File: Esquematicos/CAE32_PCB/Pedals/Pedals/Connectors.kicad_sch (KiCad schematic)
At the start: 3 parts, among them J10 ST-Link, J8 USB_C_Receptacle, J9 UART_PGR

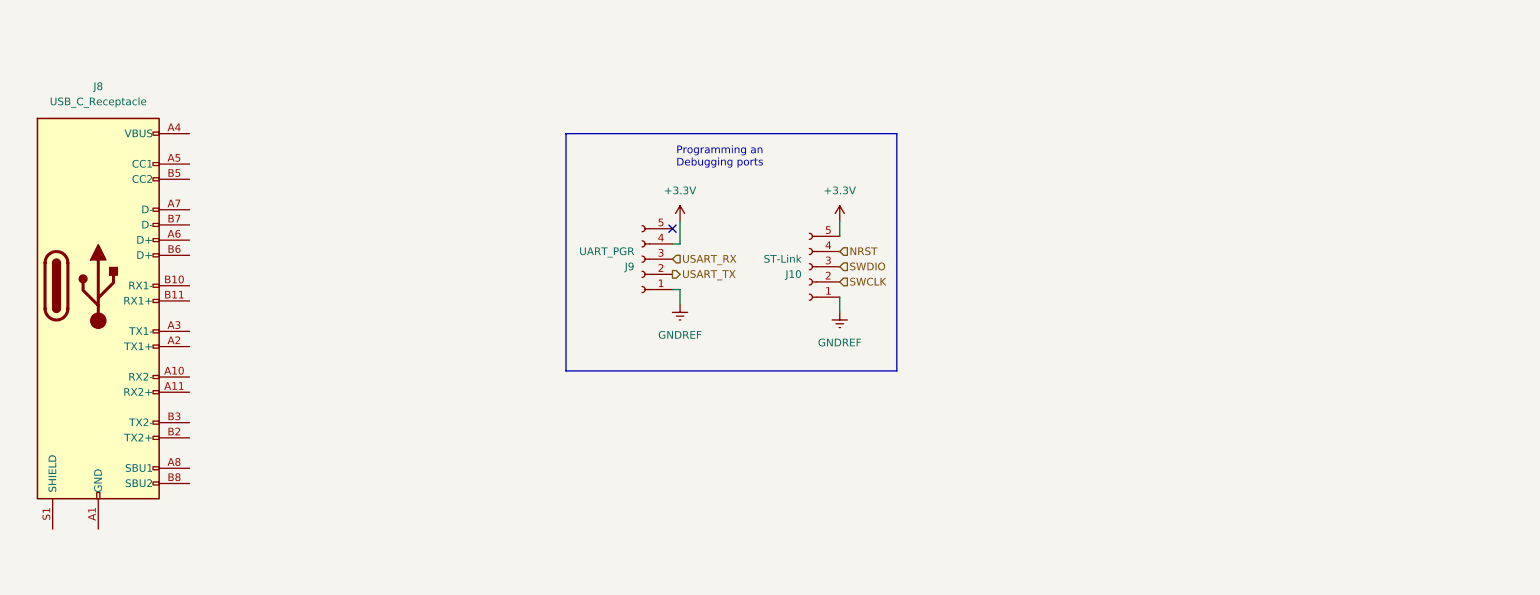
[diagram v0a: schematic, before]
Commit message: update: Primera revision de etapa ADC lista, ademas de una mejor distrubucion de componentes
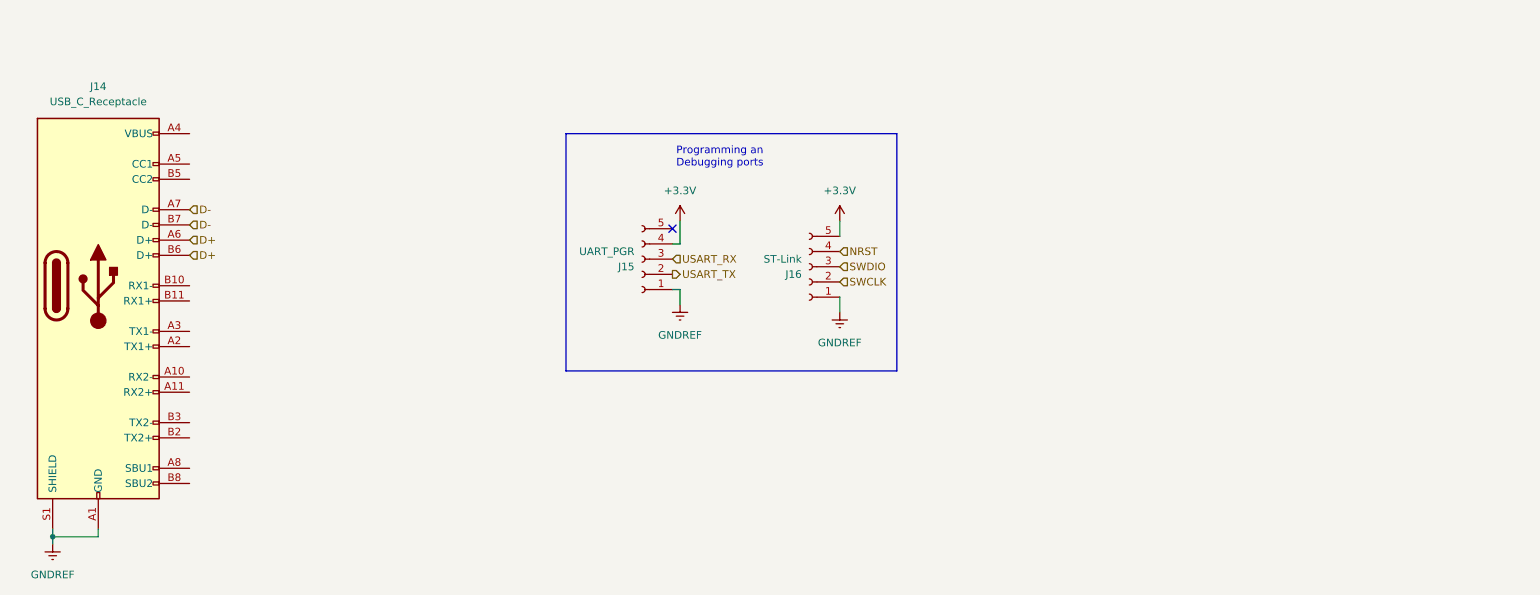
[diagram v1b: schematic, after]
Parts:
- renumbered J8 to J14, J9 to J15, J10 to J16
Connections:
- net GNDREF: now also J14.A1 (GND), J14.A12 (GND), J14.B1 (GND), J14.B12 (GND), J14.S1 (SHIELD)
- net D+: now reaches J14.A6 (D+)
- net D+: now also J14.B6 (D+)
- net D-: now reaches J14.A7 (D-)
- net D-: now also J14.B7 (D-)
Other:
- title: (none) -> CAE32 pedals
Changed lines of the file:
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@@
 (kicad_sch (version 20211123) (generator eeschema)
   (paper "A4")
+  (title_block
+    (title "CAE32 pedals")
+    (rev "2")
+    (comment 1 "Desing by: janc18")
+  )
+  (junction (at 33.655 102.87) (diameter 0) (color 0 0 0 0)
+  )
   (no_connect (at 137.16 51.435))
   (polyline (pts (xy 174.625 35.56) (xy 174.625 75.184))
@@
     (stroke (width 0) (type default) (color 0 0 0 0))
   )
+  (wire (pts (xy 33.655 101.6) (xy 33.655 102.87))
+    (stroke (width 0) (type default) (color 0 0 0 0))
+  )
   (polyline (pts (xy 119.38 75.184) (xy 174.625 75.184))
     (stroke (width 0) (type default) (color 0 0 0 0))
@@
     (stroke (width 0) (type default) (color 0 0 0 0))
   )
+  (wire (pts (xy 33.655 102.87) (xy 41.275 102.87))
+    (stroke (width 0) (type default) (color 0 0 0 0))
+  )
   (wire (pts (xy 138.43 64.135) (xy 138.43 61.595))
     (stroke (width 0) (type default) (color 0 0 0 0))
@@
     (stroke (width 0) (type default) (color 0 0 0 0))
   )
+  (wire (pts (xy 41.275 101.6) (xy 41.275 102.87))
+    (stroke (width 0) (type default) (color 0 0 0 0))
+  )
   (wire (pts (xy 165.1 50.165) (xy 165.1 52.705))
+    (stroke (width 0) (type default) (color 0 0 0 0))
+  )
+  (wire (pts (xy 33.655 102.87) (xy 33.655 104.14))
     (stroke (width 0) (type default) (color 0 0 0 0))
   )
@@
     (effects (font (size 1.27 1.27)) (justify left))
   )
+  (hierarchical_label "D-" (shape input) (at 56.515 48.26 0)
+    (effects (font (size 1.27 1.27)) (justify left))
+  )
   (hierarchical_label "NRST" (shape input) (at 165.1 55.245 0)
     (effects (font (size 1.27 1.27)) (justify left))
@@
     (effects (font (size 1.27 1.27)) (justify left))
   )
+  (hierarchical_label "D-" (shape input) (at 56.515 50.8 0)
+    (effects (font (size 1.27 1.27)) (justify left))
+  )
   (hierarchical_label "SWCLK" (shape input) (at 165.1 60.325 0)
     (effects (font (size 1.27 1.27)) (justify left))
   )
+  (hierarchical_label "D+" (shape input) (at 56.515 55.88 0)
+    (effects (font (size 1.27 1.27)) (justify left))
+  )
+  (hierarchical_label "D+" (shape input) (at 56.515 53.34 0)
+    (effects (font (size 1.27 1.27)) (justify left))
+  )
   (symbol (lib_id "power:GNDREF") (at 165.1 65.405 0) (unit 1)
     (in_bom yes) (on_board yes) (fields_autoplaced)
-    (property "Reference" "#PWR038" (id 0) (at 165.1 71.755 0)
+    (property "Reference" "#PWR053" (id 0) (at 165.1 71.755 0)
       (effects (font (size 1.27 1.27)) hide)
     )
@@
   (symbol (lib_id "Connector:USB_C_Receptacle") (at 41.275 60.96 0) (unit 1)
     (in_bom yes) (on_board yes) (fields_autoplaced)
-    (property "Reference" "J8" (id 0) (at 41.275 27.686 0))
+    (property "Reference" "J14" (id 0) (at 41.275 27.686 0))
     (property "Value" "USB_C_Receptacle" (id 1) (at 41.275 30.226 0))
     (property "Footprint" "Connector_USB:USB_C_Receptacle_Amphenol_12401548E4-2A_CircularHoles" (id 2) (at 45.085 60.96 0)
@@
   (symbol (lib_id "power:GNDREF") (at 138.43 64.135 0) (unit 1)
     (in_bom yes) (on_board yes) (fields_autoplaced)
-    (property "Reference" "#PWR036" (id 0) (at 138.43 70.485 0)
+    (property "Reference" "#PWR051" (id 0) (at 138.43 70.485 0)
       (effects (font (size 1.27 1.27)) hide)
     )
@@
   (symbol (lib_id "power:+3.3V") (at 138.43 50.165 0) (unit 1)
     (in_bom yes) (on_board yes) (fields_autoplaced)
-    (property "Reference" "#PWR035" (id 0) (at 138.43 53.975 0)
+    (property "Reference" "#PWR050" (id 0) (at 138.43 53.975 0)
       (effects (font (size 1.27 1.27)) hide)
     )
@@
     (pin "1")
   )
+  (symbol (lib_name "GNDREF_1") (lib_id "power:GNDREF") (at 33.655 104.14 0) (unit 1)
+    (in_bom yes) (on_board yes) (fields_autoplaced)
+    (property "Reference" "#PWR049" (id 0) (at 33.655 110.49 0)
+      (effects (font (size 1.27 1.27)) hide)
+    )
+    (property "Value" "GNDREF" (id 1) (at 33.655 109.22 0))
+    (property "Footprint" "" (id 2) (at 33.655 104.14 0)
+      (effects (font (size 1.27 1.27)) hide)
+    )
+    (property "Datasheet" "" (id 3) (at 33.655 104.14 0)
+      (effects (font (size 1.27 1.27)) hide)
+    )
+    (pin "1")
+  )
   (symbol (lib_id "power:+3.3V") (at 165.1 50.165 0) (unit 1)
     (in_bom yes) (on_board yes) (fields_autoplaced)
-    (property "Reference" "#PWR037" (id 0) (at 165.1 53.975 0)
+    (property "Reference" "#PWR052" (id 0) (at 165.1 53.975 0)
       (effects (font (size 1.27 1.27)) hide)
     )
@@
   (symbol (lib_id "Connector:Conn_01x05_Female") (at 132.08 56.515 180) (unit 1)
     (in_bom yes) (on_board yes)
-    (property "Reference" "J9" (id 0) (at 130.81 57.7851 0)
+    (property "Reference" "J15" (id 0) (at 130.81 57.7851 0)
       (effects (font (size 1.27 1.27)) (justify left))
     )
@@
   (symbol (lib_id "Connector:Conn_01x05_Female") (at 160.02 57.785 180) (unit 1)
     (in_bom yes) (on_board yes)
-    (property "Reference" "J10" (id 0) (at 158.75 59.0551 0)
+    (property "Reference" "J16" (id 0) (at 158.75 59.0551 0)
       (effects (font (size 1.27 1.27)) (justify left))
     )

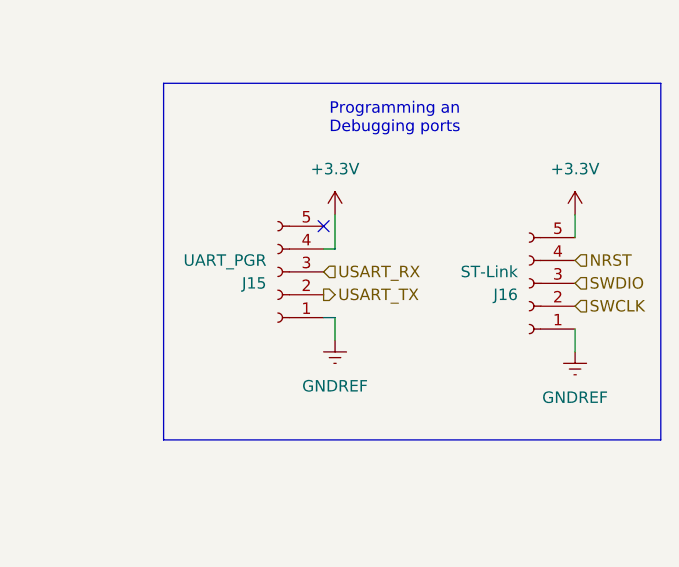
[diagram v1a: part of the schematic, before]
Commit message: update: se añade otra hoja para las celdas de carga, ademas de reorganizar todas las hojas
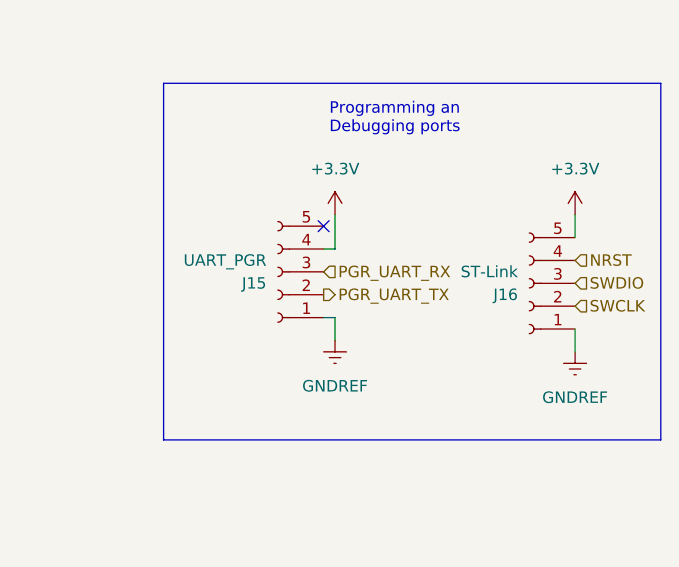
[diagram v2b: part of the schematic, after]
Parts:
- J14: footprint Connector_USB:USB_C_Receptacle_Amphenol_12401548E4-2A_CircularHoles -> Connector_USB:USB_C_Receptacle_G-Switch_GT-USB-7010ASV
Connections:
- net USART_RX renamed PGR_UART_RX
- net USART_TX renamed PGR_UART_TX
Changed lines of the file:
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@@
     (effects (font (size 1.27 1.27)) (justify left bottom))
   )
-  (hierarchical_label "USART_TX" (shape output) (at 137.16 59.055 0)
+  (hierarchical_label "PGR_UART_TX" (shape output) (at 137.16 59.055 0)
     (effects (font (size 1.27 1.27)) (justify left))
   )
@@
     (effects (font (size 1.27 1.27)) (justify left))
   )
-  (hierarchical_label "USART_RX" (shape input) (at 137.16 56.515 0)
+  (hierarchical_label "PGR_UART_RX" (shape input) (at 137.16 56.515 0)
     (effects (font (size 1.27 1.27)) (justify left))
   )
@@
   (symbol (lib_id "power:GNDREF") (at 165.1 65.405 0) (unit 1)
     (in_bom yes) (on_board yes) (fields_autoplaced)
-    (property "Reference" "#PWR053" (id 0) (at 165.1 71.755 0)
+    (property "Reference" "#PWR045" (id 0) (at 165.1 71.755 0)
       (effects (font (size 1.27 1.27)) hide)
     )
@@
     (property "Reference" "J14" (id 0) (at 41.275 27.686 0))
     (property "Value" "USB_C_Receptacle" (id 1) (at 41.275 30.226 0))
-    (property "Footprint" "Connector_USB:USB_C_Receptacle_Amphenol_12401548E4-2A_CircularHoles" (id 2) (at 45.085 60.96 0)
+    (property "Footprint" "Connector_USB:USB_C_Receptacle_G-Switch_GT-USB-7010ASV" (id 2) (at 45.085 60.96 0)
       (effects (font (size 1.27 1.27)) hide)
     )
@@
   (symbol (lib_id "power:GNDREF") (at 138.43 64.135 0) (unit 1)
     (in_bom yes) (on_board yes) (fields_autoplaced)
-    (property "Reference" "#PWR051" (id 0) (at 138.43 70.485 0)
+    (property "Reference" "#PWR043" (id 0) (at 138.43 70.485 0)
       (effects (font (size 1.27 1.27)) hide)
     )
@@
   (symbol (lib_id "power:+3.3V") (at 138.43 50.165 0) (unit 1)
     (in_bom yes) (on_board yes) (fields_autoplaced)
-    (property "Reference" "#PWR050" (id 0) (at 138.43 53.975 0)
+    (property "Reference" "#PWR042" (id 0) (at 138.43 53.975 0)
       (effects (font (size 1.27 1.27)) hide)
     )
@@
   (symbol (lib_name "GNDREF_1") (lib_id "power:GNDREF") (at 33.655 104.14 0) (unit 1)
     (in_bom yes) (on_board yes) (fields_autoplaced)
-    (property "Reference" "#PWR049" (id 0) (at 33.655 110.49 0)
+    (property "Reference" "#PWR041" (id 0) (at 33.655 110.49 0)
       (effects (font (size 1.27 1.27)) hide)
     )
@@
   (symbol (lib_id "power:+3.3V") (at 165.1 50.165 0) (unit 1)
     (in_bom yes) (on_board yes) (fields_autoplaced)
-    (property "Reference" "#PWR052" (id 0) (at 165.1 53.975 0)
+    (property "Reference" "#PWR044" (id 0) (at 165.1 53.975 0)
       (effects (font (size 1.27 1.27)) hide)
     )

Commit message: update: Componentes acomodados en la PCB
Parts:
- renumbered J14 to J15, J15 to J16, J16 to J17
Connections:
- net PGR_UART_RX: now also J16.2 (Pin_2); no longer J16.3 (Pin_3)
- net PGR_UART_TX: now also J16.3 (Pin_3); no longer J16.2 (Pin_2)
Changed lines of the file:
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@@
     (effects (font (size 1.27 1.27)) (justify left bottom))
   )
-  (hierarchical_label "PGR_UART_TX" (shape output) (at 137.16 59.055 0)
+  (hierarchical_label "PGR_UART_TX" (shape output) (at 137.16 56.515 0)
     (effects (font (size 1.27 1.27)) (justify left))
   )
@@
     (effects (font (size 1.27 1.27)) (justify left))
   )
-  (hierarchical_label "PGR_UART_RX" (shape input) (at 137.16 56.515 0)
+  (hierarchical_label "PGR_UART_RX" (shape input) (at 137.16 59.055 0)
     (effects (font (size 1.27 1.27)) (justify left))
   )
@@
   (symbol (lib_id "Connector:USB_C_Receptacle") (at 41.275 60.96 0) (unit 1)
     (in_bom yes) (on_board yes) (fields_autoplaced)
-    (property "Reference" "J14" (id 0) (at 41.275 27.686 0))
+    (property "Reference" "J15" (id 0) (at 41.275 27.686 0))
     (property "Value" "USB_C_Receptacle" (id 1) (at 41.275 30.226 0))
     (property "Footprint" "Connector_USB:USB_C_Receptacle_G-Switch_GT-USB-7010ASV" (id 2) (at 45.085 60.96 0)
@@
   (symbol (lib_id "Connector:Conn_01x05_Female") (at 132.08 56.515 180) (unit 1)
     (in_bom yes) (on_board yes)
-    (property "Reference" "J15" (id 0) (at 130.81 57.7851 0)
+    (property "Reference" "J16" (id 0) (at 130.81 57.7851 0)
       (effects (font (size 1.27 1.27)) (justify left))
     )
@@
   (symbol (lib_id "Connector:Conn_01x05_Female") (at 160.02 57.785 180) (unit 1)
     (in_bom yes) (on_board yes)
-    (property "Reference" "J16" (id 0) (at 158.75 59.0551 0)
+    (property "Reference" "J17" (id 0) (at 158.75 59.0551 0)
       (effects (font (size 1.27 1.27)) (justify left))
     )

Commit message: update: se agrega el consumo de corriente a los IC's ademas de agregar el URL y numero de parte de los componentes de LCSC en kicad
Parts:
- J16, J17: LCSC_PART (none) -> C50950
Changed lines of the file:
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@@
+      (effects (font (size 1.27 1.27)) hide)
+    )
+    (property "LCSC_PART" "C50950" (id 4) (at 132.08 56.515 0)
       (effects (font (size 1.27 1.27)) hide)
     )
@@
       (effects (font (size 1.27 1.27)) hide)
     )
+    (property "LCSC_PART" "C50950" (id 4) (at 160.02 57.785 0)
+      (effects (font (size 1.27 1.27)) hide)
+    )

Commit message: Update: esquematicos de PCB, reorganizando elementos para hacer mas compacta la pcb, ademas de agregar serigrafia e imagenes de la PCB
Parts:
- J16, J17: footprint Connector_PinSocket_2.54mm:PinSocket_1x05_P2.54mm_Horizontal -> Connector_PinSocket_2.54mm:PinSocket_1x05_P2.54mm_Vertical
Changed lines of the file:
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@@
       (effects (font (size 1.27 1.27)) (justify left))
     )
-    (property "Footprint" "Connector_PinSocket_2.54mm:PinSocket_1x05_P2.54mm_Horizontal" (id 2) (at 132.08 56.515 0)
+    (property "Footprint" "Connector_PinSocket_2.54mm:PinSocket_1x05_P2.54mm_Vertical" (id 2) (at 132.08 56.515 0)
       (effects (font (size 1.27 1.27)) hide)
     )
@@
       (effects (font (size 1.27 1.27)) (justify left))
     )
-    (property "Footprint" "Connector_PinSocket_2.54mm:PinSocket_1x05_P2.54mm_Horizontal" (id 2) (at 160.02 57.785 0)
+    (property "Footprint" "Connector_PinSocket_2.54mm:PinSocket_1x05_P2.54mm_Vertical" (id 2) (at 160.02 57.785 0)
       (effects (font (size 1.27 1.27)) hide)
     )

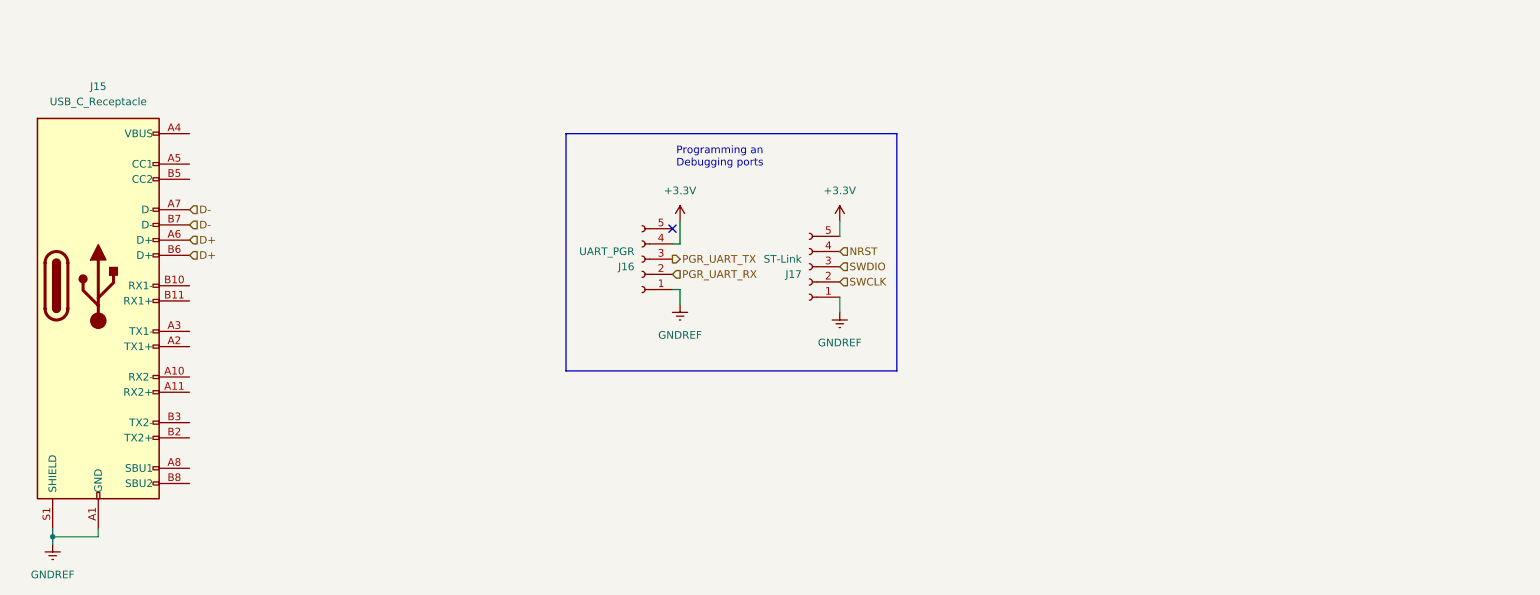
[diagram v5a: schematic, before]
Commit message: update: se crea la primera revisión de la PCB
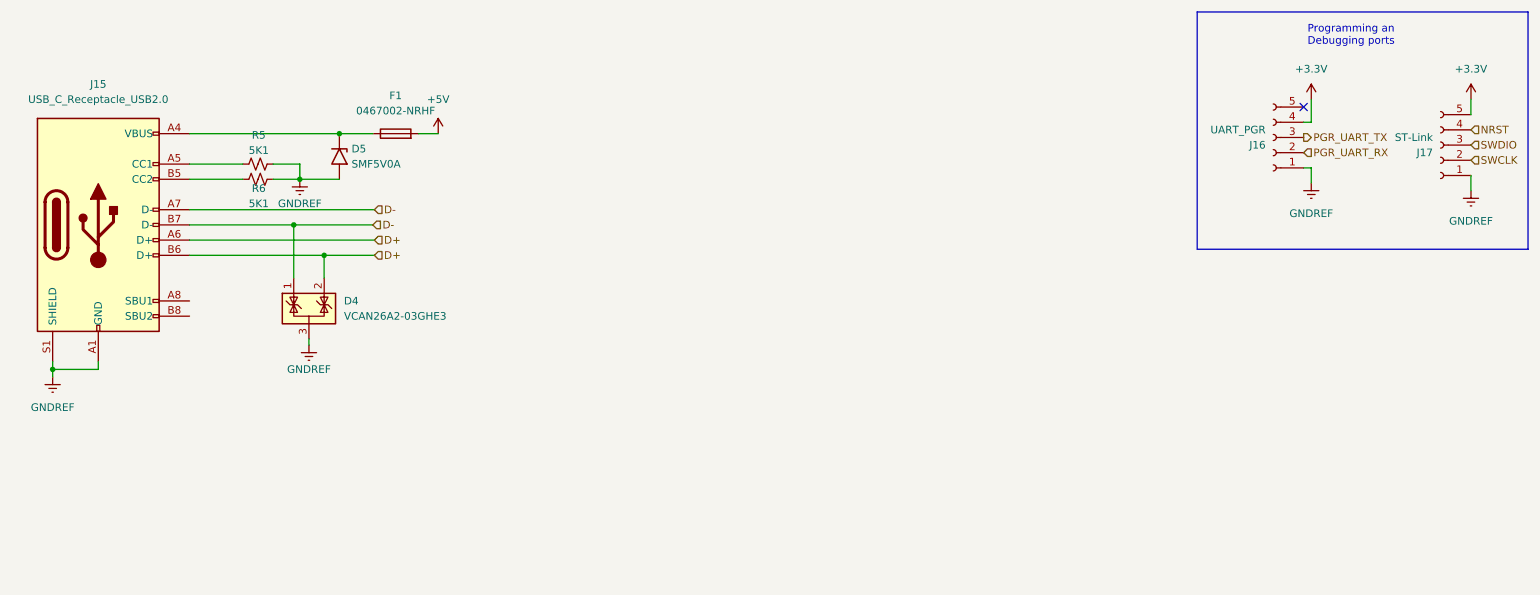
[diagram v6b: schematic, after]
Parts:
- removed J15: USB_C_Receptacle, Connector_USB:USB_C_Receptacle_G-Switch_GT-USB-7010ASV, symbol Connector:USB_C_Receptacle
- added D4: VCAN26A2-03GHE3, Package_TO_SOT_SMD:SOT-323_SC-70, symbol Power_Protection:NUP2105L
- added D5: SMF5V0A, Diode_SMD:D_SOD-123, symbol Diode:SMF5V0A
- added F1: 0467002-NRHF, Fuse:Fuse_0603_1608Metric_Pad1.05x0.95mm_HandSolder, symbol Device:Fuse
- added J15: USB_C_Receptacle_USB2.0, Connector_USB:USB_C_Receptacle_HRO_TYPE-C-31-M-12, symbol Connector:USB_C_Receptacle_USB2.0
- added R5, R6: 5K1, Resistor_SMD:R_0603_1608Metric_Pad0.98x0.95mm_HandSolder, symbol Device:R_Small_US
- J16, J17: Item (none) -> C50950; Qty (none) -> 1; Vendor (none) -> C50950
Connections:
- net D+: now also D4.2 (K), J15.A6 (D+), J15.B6 (D+)
- net D-: now also D4.1 (K), J15.A7 (D-), J15.B7 (D-)
- net GNDREF: now also D4.3 (A), D5.2 (A2), J15.A1 (GND), J15.A12 (GND), J15.B1 (GND), J15.B12 (GND), J15.S1 (SHIELD), R5.2, R6.2
- new net: D5.1 (A1), F1.1, J15.A4 (VBUS), J15.A9 (VBUS), J15.B4 (VBUS), J15.B9 (VBUS)
- new net: J15.A5 (CC1), R5.1
- new net: J15.B5 (CC2), R6.1
- new net +5V: F1.2
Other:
- moved on the sheet: J16, J17

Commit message: add: se añade un fusible extra para proteger el circuito de 5v al regulador de voltage de 3v3
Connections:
- no-connect marks 1 -> 3
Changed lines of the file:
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@@
   (junction (at 73.914 50.8) (diameter 0) (color 0 0 0 0)
   )
+  (no_connect (at 56.515 66.04))
   (no_connect (at 242.57 31.115))
+  (no_connect (at 56.515 63.5))
   (wire (pts (xy 78.994 55.88) (xy 87.376 55.88))
     (stroke (width 0) (type default) (color 0 0 0 0))
